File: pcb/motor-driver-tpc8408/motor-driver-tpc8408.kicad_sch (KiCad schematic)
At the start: 13 parts, among them J1 Conn_01x12, U1 TPC8408, U2 TPC8408, U3 74HC00

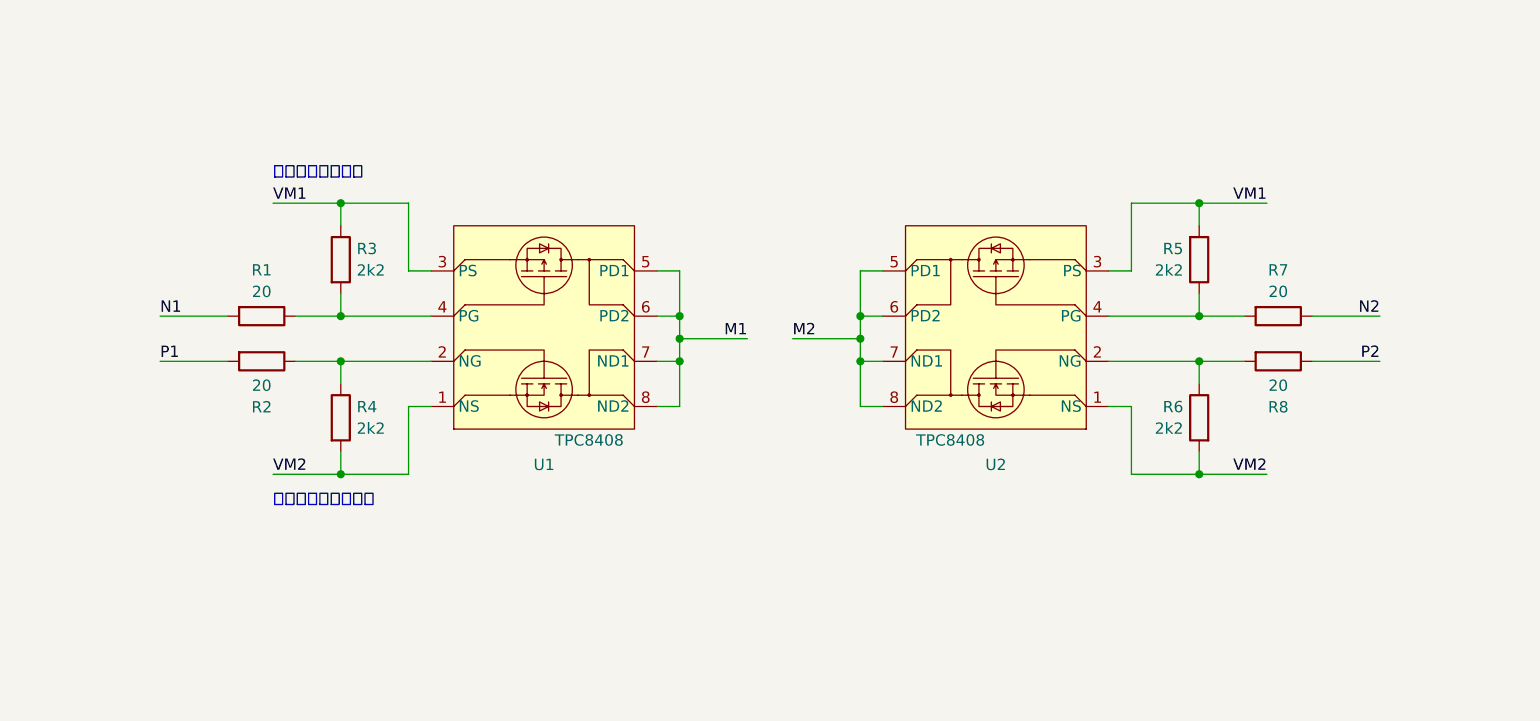
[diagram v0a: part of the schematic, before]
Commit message: 配線が間違っていたのを修正した
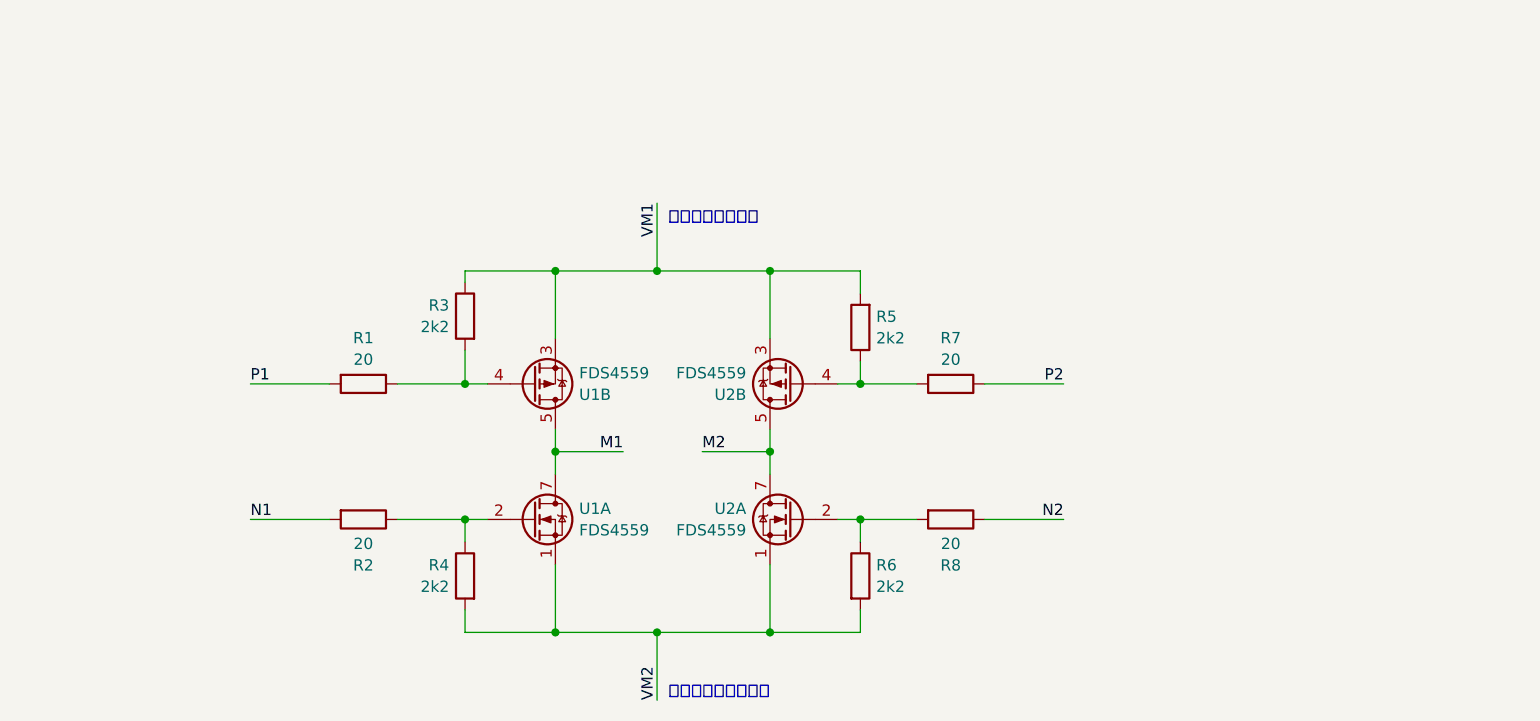
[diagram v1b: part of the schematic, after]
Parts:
- removed U1, U2: TPC8408, Package_SO:SOP-8_3.9x4.9mm_P1.27mm, symbol MyLib:TPC8408
- added U1, U2: FDS4559, Package_SO:SOIC-8_3.9x4.9mm_P1.27mm, symbol Transistor_FET:FDS4559
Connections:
- net IN_A: now also R8.1; no longer R7.1
- net IN_B: now also R2.2; no longer R1.2
- net M1: now also U1.5 (D), U1.6 (D), U1.7 (D), U1.8 (D)
- net M2: now also U2.5 (D), U2.6 (D), U2.7 (D), U2.8 (D)
- net P1: now also R1.2; no longer R2.2
- net P2: now also R7.1; no longer R8.1
- net VM1: now also U1.3 (1), U2.3 (1)
- net VM2: now also U1.1 (S), U2.1 (S)
- net at R1.1, R3.2: now also U1.4 (G)
- net at R2.1, R4.1: now also U1.2 (G)
- net at R5.1, R7.2: now also U2.4 (G)
- net at R6.1, R8.2: now also U2.2 (G)
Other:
- moved on the sheet: R1, R2, R3, R4, R5, R6, R7, R8
